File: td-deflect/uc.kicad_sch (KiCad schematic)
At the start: 18 parts, among them J4 Conn_ARM_JTAG_SWD_10, J6 Conn_01x06_Male, U12 LM1117-5.0, U2 STM32G474xx, U3 INA193, U4 TPS70933, X1 SG-8002CA

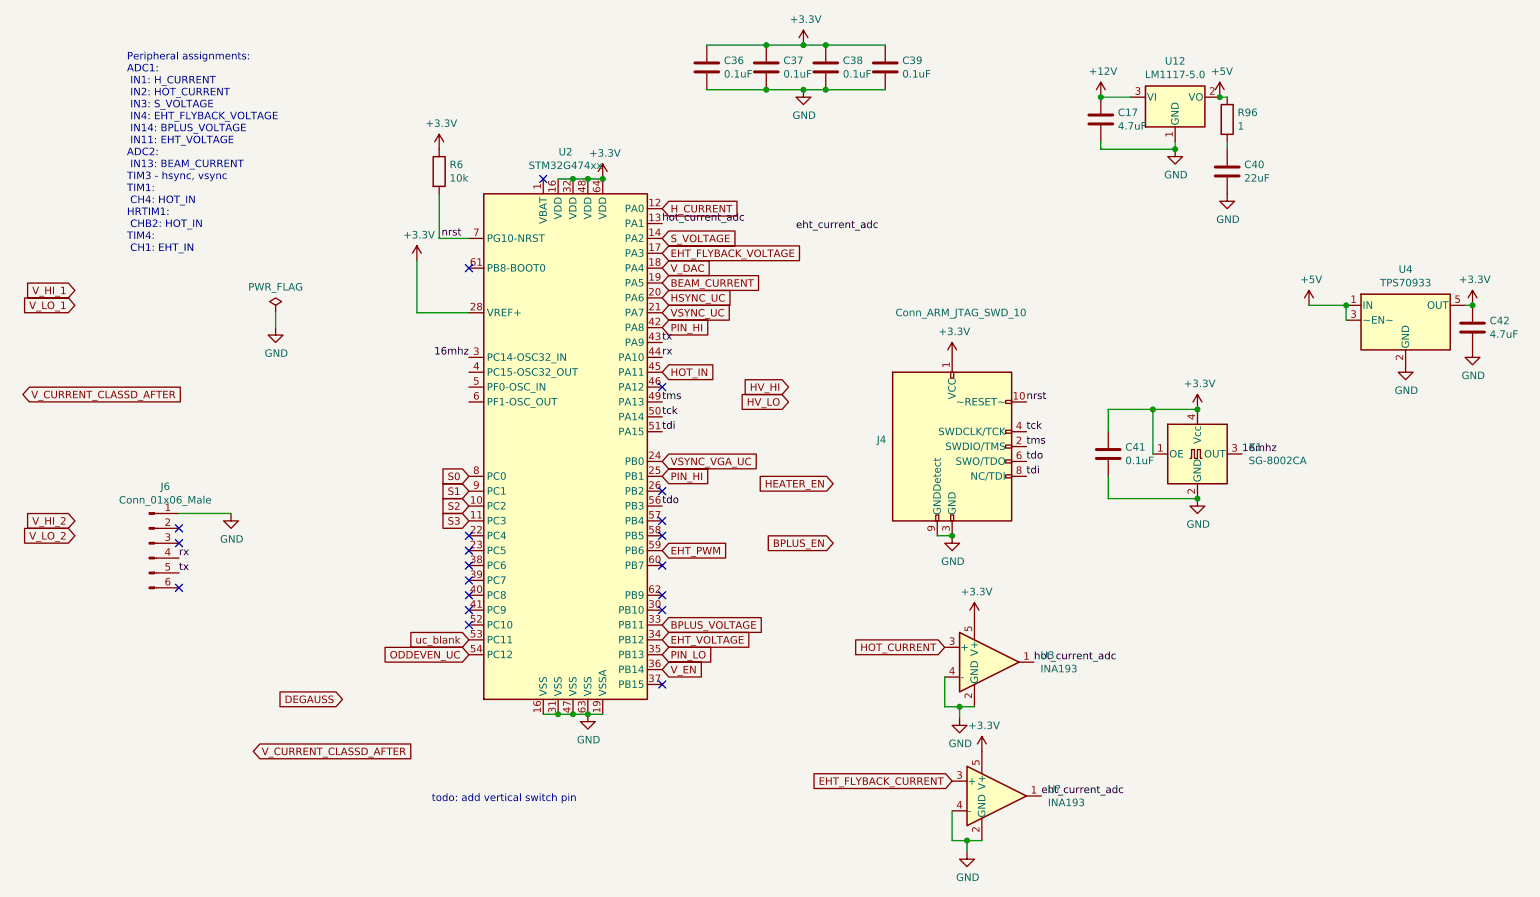
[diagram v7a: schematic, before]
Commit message: connect more uc pins
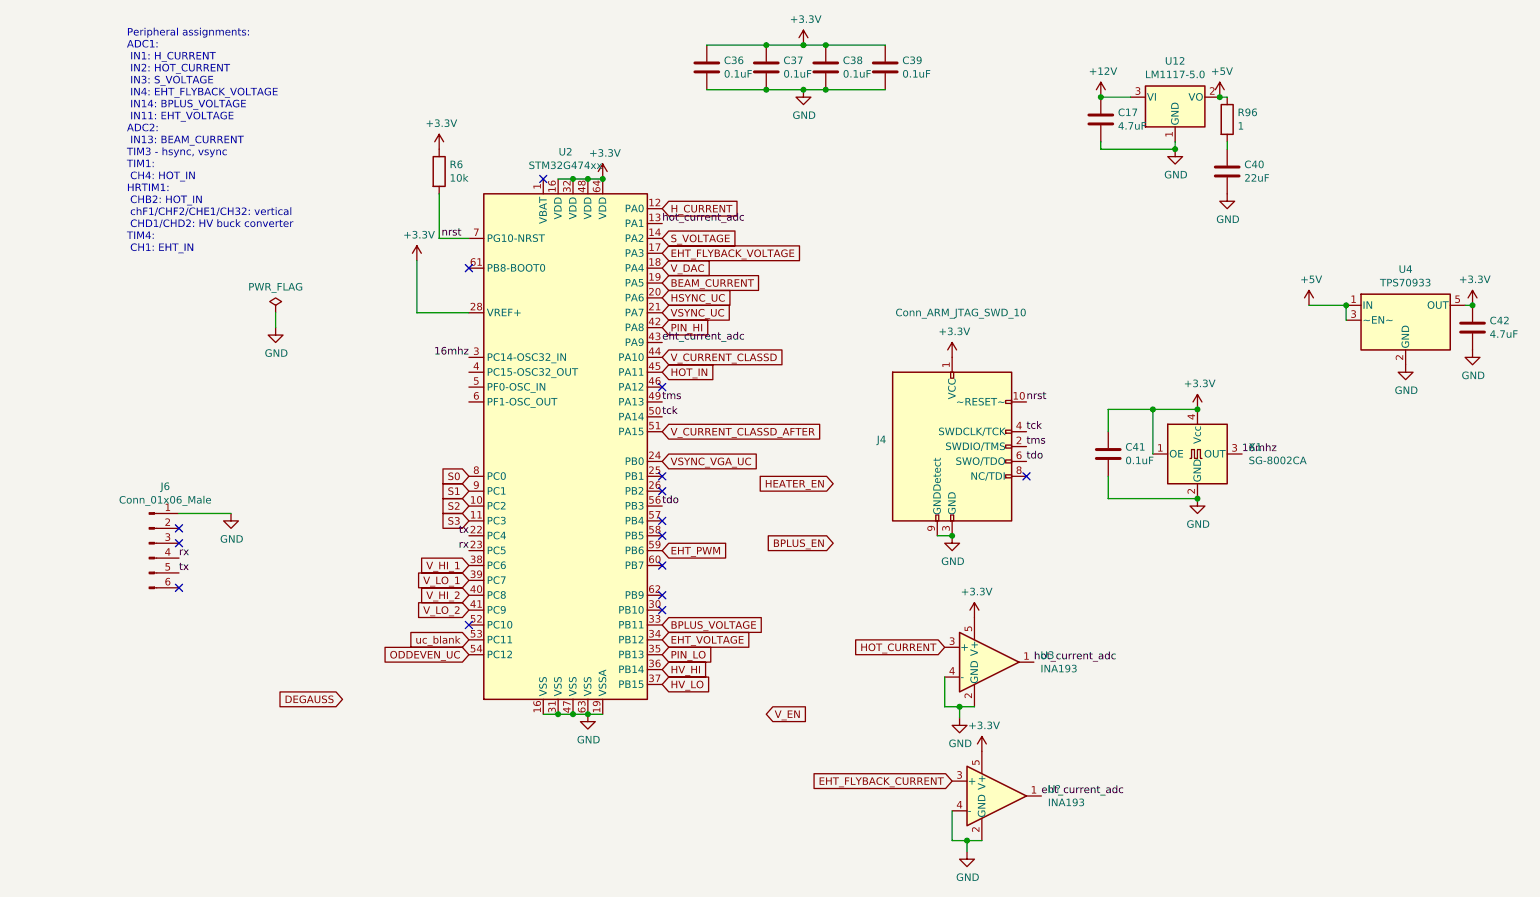
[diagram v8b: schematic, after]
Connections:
- net HV_HI: now also U2.36 (PB14)
- net HV_LO: now also U2.37 (PB15)
- net PIN_HI: no longer U2.25 (PB1)
- net V_CURRENT_CLASSD_AFTER: now also U2.51 (PA15)
- net V_EN: no longer U2.36 (PB14)
- net V_HI_1: now also U2.38 (PC6)
- net V_HI_2: now also U2.40 (PC8)
- net V_LO_1: now also U2.39 (PC7)
- net V_LO_2: now also U2.41 (PC9)
- net eht_current_adc: now also U2.43 (PA9)
- net rx: now also U2.23 (PC5); no longer U2.44 (PA10)
- net tx: now also U2.22 (PC4); no longer U2.43 (PA9)
- net tdi: no longer names the net of J4.8 (NC/TDI)
- net tdi: no longer U2.51 (PA15)
- new net V_CURRENT_CLASSD: U2.44 (PA10)
- no-connect marks 20 -> 15
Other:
- note added: "Peripheral assignments: ADC1: IN1: H_CURRENT IN2: HOT_CURRENT IN3: S_VOLTAGE IN4: EHT_FLYBACK_VOLTAGE IN14: BPLUS_VOLTAGE IN11: EHT_VOLTAGE ADC2: IN13: BEAM_CURRENT TIM3 - hsync, vsync TIM1: CH4: HOT_IN HRTIM1: CHB2: HOT_IN chF1/CHF2/CHE1/CH32: vertical CHD1/CHD2: HV buck converter TIM4: CH1: EHT_IN"
- note removed: "Peripheral assignments: ADC1: IN1: H_CURRENT IN2: HOT_CURRENT IN3: S_VOLTAGE IN4: EHT_FLYBACK_VOLTAGE IN14: BPLUS_VOLTAGE IN11: EHT_VOLTAGE ADC2: IN13: BEAM_CURRENT TIM3 - hsync, vsync TIM1: CH4: HOT_IN HRTIM1: CHB2: HOT_IN TIM4: CH1: EHT_IN"
- note removed: "todo: add vertical switch pin"
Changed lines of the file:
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@@
   (no_connect (at 50.8 106.68))
   (no_connect (at 133.35 102.87))
-  (no_connect (at 100.33 107.95))
-  (no_connect (at 100.33 113.03))
   (no_connect (at 50.8 104.14))
-  (no_connect (at 133.35 130.81))
   (no_connect (at 133.35 97.79))
   (no_connect (at 133.35 118.11))
   (no_connect (at 50.8 114.3))
   (no_connect (at 113.03 44.45))
+  (no_connect (at 195.58 95.25))
   (no_connect (at 133.35 110.49))
-  (no_connect (at 100.33 110.49))
   (no_connect (at 100.33 120.65))
   (no_connect (at 133.35 105.41))
   (no_connect (at 100.33 59.69))
   (no_connect (at 133.35 115.57))
-  (no_connect (at 100.33 115.57))
   (no_connect (at 133.35 80.01))
-  (no_connect (at 100.33 118.11))
-  (no_connect (at 100.33 105.41))
+  (no_connect (at 133.35 95.25))
   (wire (pts (xy 208.28 39.37) (xy 220.98 39.37))
     (stroke (width 0) (type solid) (color 0 0 0 0))
@@
     (stroke (width 0) (type default) (color 0 0 0 0))
   )
-  (text "Peripheral assignments:\nADC1:\n IN1: H_CURRENT\n IN2: HOT_CURRENT\n IN3: S_VOLTAGE\n IN4: EHT_FLYBACK_VOLTAGE\n IN14: BPLUS_VOLTAGE\n IN11: EHT_VOLTAGE\nADC2:\n IN13: BEAM_CURRENT\nTIM3 - hsync, vsync\nTIM1:\n CH4: HOT_IN\nHRTIM1:\n CHB2: HOT_IN\nTIM4:\n CH1: EHT_IN"
+  (text "Peripheral assignments:\nADC1:\n IN1: H_CURRENT\n IN2: HOT_CURRENT\n IN3: S_VOLTAGE\n IN4: EHT_FLYBACK_VOLTAGE\n IN14: BPLUS_VOLTAGE\n IN11: EHT_VOLTAGE\nADC2:\n IN13: BEAM_CURRENT\nTIM3 - hsync, vsync\nTIM1:\n CH4: HOT_IN\nHRTIM1:\n CHB2: HOT_IN\n chF1/CHF2/CHE1/CH32: vertical\n CHD1/CHD2: HV buck converter\nTIM4:\n CH1: EHT_IN"
     (at 41.91 57.15 0)
     (effects (font (size 1.27 1.27)) (justify left bottom))
   )
-  (text "todo: add vertical switch pin" (at 93.98 151.13 0)
-    (effects (font (size 1.27 1.27)) (justify left bottom))
-  )
   (label "tx" (at 50.8 111.76 0)
     (effects (font (size 1.27 1.27)) (justify left bottom))
@@
     (effects (font (size 1.27 1.27)) (justify left bottom))
   )
-  (label "tdi" (at 195.58 95.25 0)
-    (effects (font (size 1.27 1.27)) (justify left bottom))
-  )
   (label "eht_current_adc" (at 198.12 149.86 0)
     (effects (font (size 1.27 1.27)) (justify left bottom))
   )
-  (label "tx" (at 133.35 72.39 0)
-    (effects (font (size 1.27 1.27)) (justify left bottom))
-  )
-  (label "eht_current_adc" (at 156.21 53.34 0)
+  (label "tx" (at 100.33 105.41 180)
+    (effects (font (size 1.27 1.27)) (justify right bottom))
+  )
+  (label "eht_current_adc" (at 133.35 72.39 0)
     (effects (font (size 1.27 1.27)) (justify left bottom))
   )
@@
     (effects (font (size 1.27 1.27)) (justify right bottom))
   )
-  (label "tdi" (at 133.35 87.63 0)
-    (effects (font (size 1.27 1.27)) (justify left bottom))
-  )
   (label "tdo" (at 133.35 100.33 0)
     (effects (font (size 1.27 1.27)) (justify left bottom))
@@
     (effects (font (size 1.27 1.27)) (justify left bottom))
   )
-  (label "rx" (at 133.35 74.93 0)
-    (effects (font (size 1.27 1.27)) (justify left bottom))
-  )
-  (global_label "PIN_HI" (shape input) (at 133.35 95.25 0) (fields_autoplaced)
-    (effects (font (size 1.27 1.27)) (justify left))
-    (property "Intersheet References" "${INTERSHEET_REFS}" (id 0) (at 0 25.4 0)
-      (effects (font (size 1.27 1.27)) hide)
-    )
+  (label "rx" (at 100.33 107.95 180)
+    (effects (font (size 1.27 1.27)) (justify right bottom))
   )
   (global_label "EHT_FLYBACK_VOLTAGE" (shape input) (at 133.35 57.15 0) (fields_autoplaced)
@@
     )
   )
-  (global_label "V_CURRENT_CLASSD_AFTER" (shape input) (at 24.13 81.28 0) (fields_autoplaced)
-    (effects (font (size 1.27 1.27)) (justify left))
-    (property "Intersheet References" "${INTERSHEET_REFS}" (id 0) (at 51.6728 81.2006 0)
-      (effects (font (size 1.27 1.27)) (justify left) hide)
-    )
-  )
-  (global_label "V_LO_1" (shape input) (at 33.02 66.04 180) (fields_autoplaced)
-    (effects (font (size 1.27 1.27)) (justify right))
-    (property "Intersheet References" "${INTERSHEET_REFS}" (id 0) (at 24.1039 65.9606 0)
-      (effects (font (size 1.27 1.27)) (justify right) hide)
-    )
-  )
-  (global_label "HV_HI" (shape input) (at 154.94 80.01 180) (fields_autoplaced)
-    (effects (font (size 1.27 1.27)) (justify right))
-    (property "Intersheet References" "${INTERSHEET_REFS}" (id 0) (at 147.2939 79.9306 0)
-      (effects (font (size 1.27 1.27)) (justify right) hide)
+  (global_label "V_CURRENT_CLASSD_AFTER" (shape input) (at 133.35 87.63 0) (fields_autoplaced)
+    (effects (font (size 1.27 1.27)) (justify left))
+    (property "Intersheet References" "${INTERSHEET_REFS}" (id 0) (at 160.8928 87.5506 0)
+      (effects (font (size 1.27 1.27)) (justify left) hide)
+    )
+  )
+  (global_label "V_LO_1" (shape input) (at 100.33 113.03 180) (fields_autoplaced)
+    (effects (font (size 1.27 1.27)) (justify right))
+    (property "Intersheet References" "${INTERSHEET_REFS}" (id 0) (at 91.4139 112.9506 0)
+      (effects (font (size 1.27 1.27)) (justify right) hide)
+    )
+  )
+  (global_label "HV_HI" (shape input) (at 133.35 128.27 0) (fields_autoplaced)
+    (effects (font (size 1.27 1.27)) (justify left))
+    (property "Intersheet References" "${INTERSHEET_REFS}" (id 0) (at 140.9961 128.3494 0)
+      (effects (font (size 1.27 1.27)) (justify left) hide)
     )
   )
@@
     )
   )
-  (global_label "V_HI_1" (shape input) (at 33.02 63.5 180) (fields_autoplaced)
-    (effects (font (size 1.27 1.27)) (justify right))
-    (property "Intersheet References" "${INTERSHEET_REFS}" (id 0) (at 24.5272 63.4206 0)
+  (global_label "V_HI_1" (shape input) (at 100.33 110.49 180) (fields_autoplaced)
+    (effects (font (size 1.27 1.27)) (justify right))
+    (property "Intersheet References" "${INTERSHEET_REFS}" (id 0) (at 91.8372 110.4106 0)
       (effects (font (size 1.27 1.27)) (justify right) hide)
     )
@@
     )
   )
-  (global_label "V_HI_2" (shape input) (at 33.02 102.87 180) (fields_autoplaced)
-    (effects (font (size 1.27 1.27)) (justify right))
-    (property "Intersheet References" "${INTERSHEET_REFS}" (id 0) (at 24.5272 102.7906 0)
+  (global_label "V_HI_2" (shape input) (at 100.33 115.57 180) (fields_autoplaced)
+    (effects (font (size 1.27 1.27)) (justify right))
+    (property "Intersheet References" "${INTERSHEET_REFS}" (id 0) (at 91.8372 115.4906 0)
       (effects (font (size 1.27 1.27)) (justify right) hide)
     )
@@
     )
   )
-  (global_label "V_CURRENT_CLASSD_AFTER" (shape input) (at 63.5 142.24 0) (fields_autoplaced)
-    (effects (font (size 1.27 1.27)) (justify left))
-    (property "Intersheet References" "${INTERSHEET_REFS}" (id 0) (at 91.0428 142.1606 0)
+  (global_label "V_CURRENT_CLASSD" (shape input) (at 133.35 74.93 0) (fields_autoplaced)
+    (effects (font (size 1.27 1.27)) (justify left))
+    (property "Intersheet References" "${INTERSHEET_REFS}" (id 0) (at 154.3613 74.8506 0)
       (effects (font (size 1.27 1.27)) (justify left) hide)
     )
@@
     )
   )
-  (global_label "V_EN" (shape input) (at 133.35 128.27 0) (fields_autoplaced)
-    (effects (font (size 1.27 1.27)) (justify left))
-    (property "Intersheet References" "${INTERSHEET_REFS}" (id 0) (at 140.2099 128.1906 0)
+  (global_label "V_EN" (shape input) (at 151.13 135.89 0) (fields_autoplaced)
+    (effects (font (size 1.27 1.27)) (justify left))
+    (property "Intersheet References" "${INTERSHEET_REFS}" (id 0) (at 157.9899 135.8106 0)
       (effects (font (size 1.27 1.27)) (justify left) hide)
     )
@@
     )
   )
-  (global_label "V_LO_2" (shape input) (at 33.02 105.41 180) (fields_autoplaced)
-    (effects (font (size 1.27 1.27)) (justify right))
-    (property "Intersheet References" "${INTERSHEET_REFS}" (id 0) (at 24.1039 105.3306 0)
+  (global_label "V_LO_2" (shape input) (at 100.33 118.11 180) (fields_autoplaced)
+    (effects (font (size 1.27 1.27)) (justify right))
+    (property "Intersheet References" "${INTERSHEET_REFS}" (id 0) (at 91.4139 118.0306 0)
       (effects (font (size 1.27 1.27)) (justify right) hide)
     )
@@
     )
   )
-  (global_label "HV_LO" (shape input) (at 154.94 82.55 180) (fields_autoplaced)
-    (effects (font (size 1.27 1.27)) (justify right))
-    (property "Intersheet References" "${INTERSHEET_REFS}" (id 0) (at 146.8706 82.4706 0)
-      (effects (font (size 1.27 1.27)) (justify right) hide)
-    )
-  )
+  (global_label "HV_LO" (shape input) (at 133.35 130.81 0) (fields_autoplaced)
+    (effects (font (size 1.27 1.27)) (justify left))
+    (property "Intersheet References" "${INTERSHEET_REFS}" (id 0) (at 141.4194 130.8894 0)
+      (effects (font (size 1.27 1.27)) (justify left) hide)
+    )
+  )
